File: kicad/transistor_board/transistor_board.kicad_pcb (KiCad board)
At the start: 2 copper layers, 25.4 x 38.1 mm, 17 parts, among them J1 Conn_01x10, J2 Conn_01x02, J3 Conn_01x02, Q1 MMBF170, Q2 MMBF170, Q3 MMBF170, Q4 MMBF170, U2 ESP32-cam, U3 LM7805_TO220

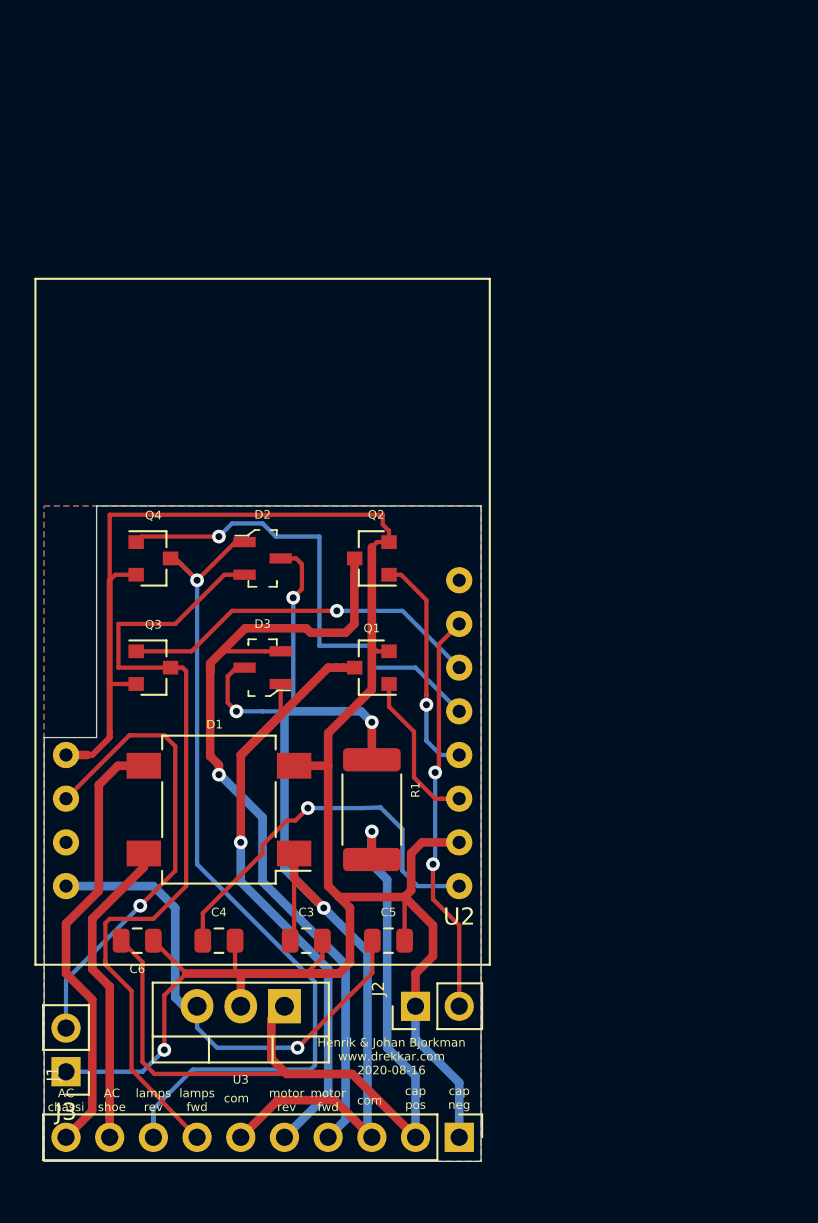
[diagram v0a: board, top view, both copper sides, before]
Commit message: Transistors failed, need to use bigger, such as D-Pak (TO252AA)
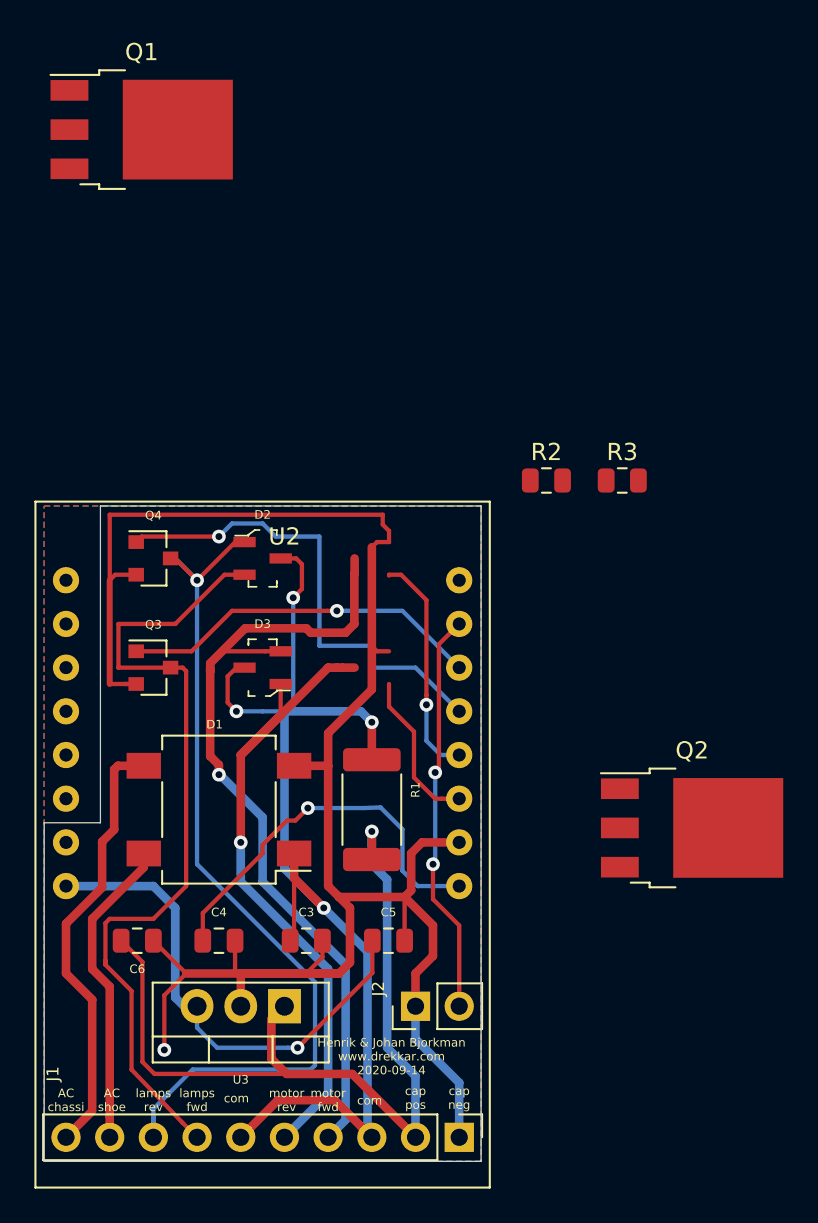
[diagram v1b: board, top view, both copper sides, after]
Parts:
- removed J3: Conn_01x02, Connector_PinHeader_2.54mm:PinHeader_1x02_P2.54mm_Vertical
- added R2: R, Resistor_SMD:R_0805_2012Metric, F.Cu at (142.2, 95.8)
- added R3: R, Resistor_SMD:R_0805_2012Metric, F.Cu at (146.6, 95.8)
- Q1, Q2: footprint Package_TO_SOT_SMD:SOT-23 -> Package_TO_SOT_SMD:TO-252-3_TabPin2
- U2: footprint eit_footprints:ESP32-CAM_12pin -> eit_footprints:ESP32-CAM
- moved Q1 34.0 mm to (118.7, 75.4), turned to 0 degrees
- moved Q2 24.3 mm to (150.7, 116.0), turned to 0 degrees
- moved U2 3.59 mm to (127.0, 109.2), turned to 0 degrees
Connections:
- U2 pad 13: GND -> Net-(U2-Pad13)
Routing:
- net Net-(U2-Pad14): track 27.2 -> 0.00 mm, vias 1 -> 0
- net Net-(U2-Pad12): track 0.00 -> 13.3 mm, vias 0 -> 1
- net Net-(Q2-Pad1): track 13.3 -> 0.00 mm, vias 1 -> 0
- net GND: track 140.3 -> 128.0 mm
- net Net-(U2-Pad11): track 0.00 -> 9.18 mm
- net Net-(Q1-Pad1): track 9.18 -> 0.00 mm
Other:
- outline, holes or cut-outs redrawn
- board text added: "Henrik & Johan Bjorkman www.drekkar.com 2020-09-14"
- board text removed: "Henrik & Johan Bjorkman www.drekkar.com 2020-08-16"

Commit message: Working on bigger transistors
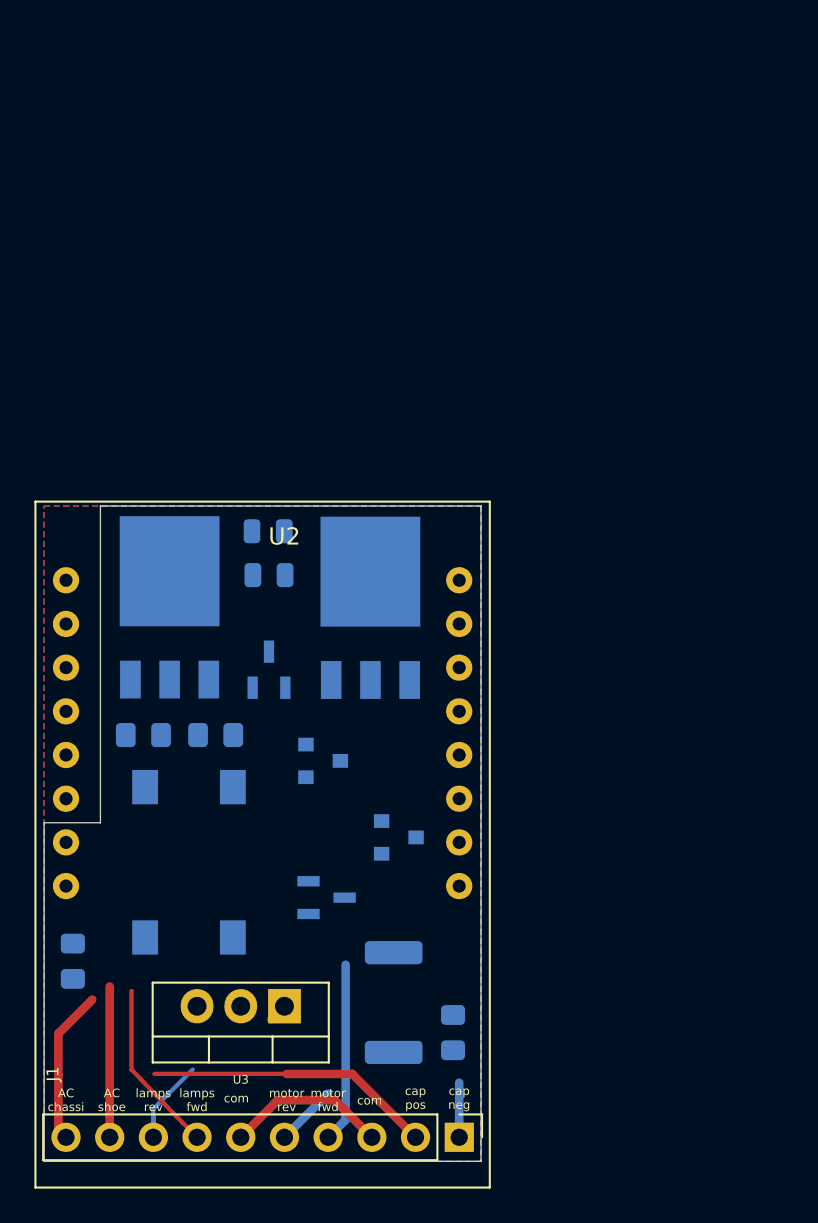
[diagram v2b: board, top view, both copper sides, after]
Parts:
- removed J2: Conn_01x02, Connector_PinHeader_2.54mm:PinHeader_1x02_P2.54mm_Vertical
- C3, C4, C5, C6: footprint Capacitor_SMD:C_0805_2012Metric -> Capacitor_SMD:C_0805_2012Metric_Pad1.15x1.40mm_HandSolder; moved to B.Cu
- D1, D2, D3, Q1, Q2, Q3, Q4, R1, R2, R3: moved to B.Cu
- moved Q2 33.0 mm to (120.3, 103.2), turned to 90 degrees
- moved Q1 30.8 mm to (132.0, 103.2), turned to 90 degrees
- moved R3 21.3 mm to (126.1, 101.3), turned to 180 degrees
- moved D2 20.1 mm to (129.4, 120.0)
- moved C6 19.1 mm to (136.8, 127.9), turned to 270 degrees
- moved C5 18.4 mm to (114.7, 123.8), turned to 270 degrees
- moved Q3 17.4 mm to (133.7, 116.5)
- moved R2 16.4 mm to (126.0, 98.8)
- moved Q4 15.4 mm to (129.2, 112.1)
- moved C3 13.1 mm to (123.0, 110.6)
- moved C4 12.7 mm to (118.8, 110.6)
- moved R1 11.3 mm to (133.3, 126.2), turned to 270 degrees
- moved D1 3.52 mm to (121.5, 118.0), turned to 270 degrees
- moved D3 0.39 mm to (126.1, 106.8), turned to 90 degrees
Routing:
- net GND: track 128.0 -> 3.18 mm, vias 1 -> 0
- net Net-(C3-Pad1): track 69.1 -> 9.77 mm, vias 4 -> 0
- net Net-(D2-Pad1): track 51.9 -> 6.09 mm, vias 1 -> 0
- net Net-(D2-Pad2): track 48.0 -> 10.1 mm
- net Net-(D3-Pad2): track 48.2 -> 10.5 mm, vias 1 -> 0
- net Net-(D3-Pad1): track 39.2 -> 3.59 mm, vias 1 -> 0
- net Net-(C6-Pad2): track 50.4 -> 17.5 mm, vias 1 -> 0
- net Net-(C5-Pad1): track 29.8 -> 0.76 mm, vias 1 -> 0
- net Net-(Q4-Pad1): track 28.3 -> 0.00 mm, vias 1 -> 0
- net Net-(J2-Pad2): track 23.5 -> 0.00 mm, vias 2 -> 0
- net Net-(C4-Pad1): track 22.6 -> 0.00 mm, vias 1 -> 0
- net Net-(Q3-Pad1): track 21.1 -> 0.00 mm, vias 1 -> 0
- net Net-(D1-Pad3): track 25.7 -> 9.01 mm
- net Net-(U2-Pad12): track 13.3 -> 0.00 mm, vias 1 -> 0
- net Net-(D1-Pad4): track 18.2 -> 8.76 mm
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
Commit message: Working on bigger transistors
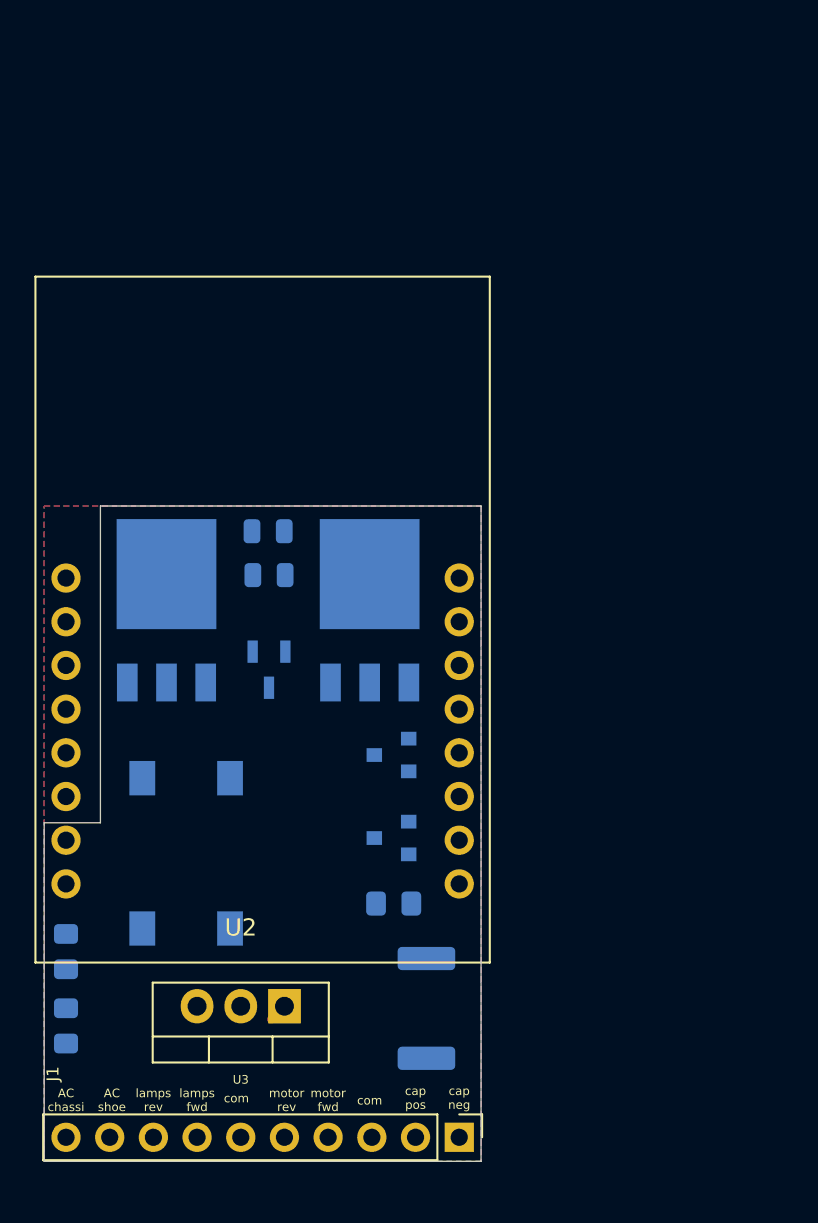
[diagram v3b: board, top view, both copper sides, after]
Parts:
- removed C4: C, Capacitor_SMD:C_0805_2012Metric_Pad1.15x1.40mm_HandSolder
- removed D2: D_x2_KCom_AAK, digikey-footprints:SOT-23-3
- moved C3 19.0 mm to (114.3, 127.5), turned to 90 degrees
- moved Q1 11.9 mm to (120.1, 103.3)
- moved Q2 11.6 mm to (132.0, 103.3)
- moved C6 8.26 mm to (133.3, 120.4), turned to 0 degrees
- moved Q4 3.99 mm to (133.2, 111.8), turned to 180 degrees
- moved U2 3.50 mm to (124.5, 111.6), turned to 180 degrees
- moved R1 1.94 mm to (135.3, 126.5), turned to 90 degrees
- moved C5 0.69 mm to (114.3, 123.2)
- moved D1 0.55 mm to (121.3, 117.5)
- moved Q3 0.43 mm to (133.2, 116.6), turned to 180 degrees
- turned D3 to 270 degrees
- turned R2 to 180 degrees
- turned R3 to 0 degrees
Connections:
- J1 pad 10: Net-(D1-Pad3) -> Net-(D1-Pad4)
- J1 pad 9: Net-(D1-Pad4) -> Net-(D1-Pad3)
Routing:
- net Net-(C6-Pad2): track 17.5 -> 1.08 mm
- net Net-(D3-Pad2): track 10.5 -> 0.00 mm
- net Net-(J1-Pad7): track 10.1 -> 0.00 mm
- net Net-(C3-Pad1): track 9.77 -> 0.00 mm
- net Net-(D1-Pad3): track 9.01 -> 0.00 mm
- net Net-(D1-Pad4): track 8.76 -> 0.64 mm
- net Net-(J1-Pad8): track 6.09 -> 0.00 mm
- net Net-(D3-Pad1): track 3.59 -> 0.00 mm
- net GND: track 3.18 -> 0.00 mm
- added copper zone on B.Cu, net GND
- added copper zone on F.Cu, net Net-(C3-Pad1)
- removed copper zone on F.Cu, net GND
- removed copper zone on B.Cu, net Net-(C3-Pad1)

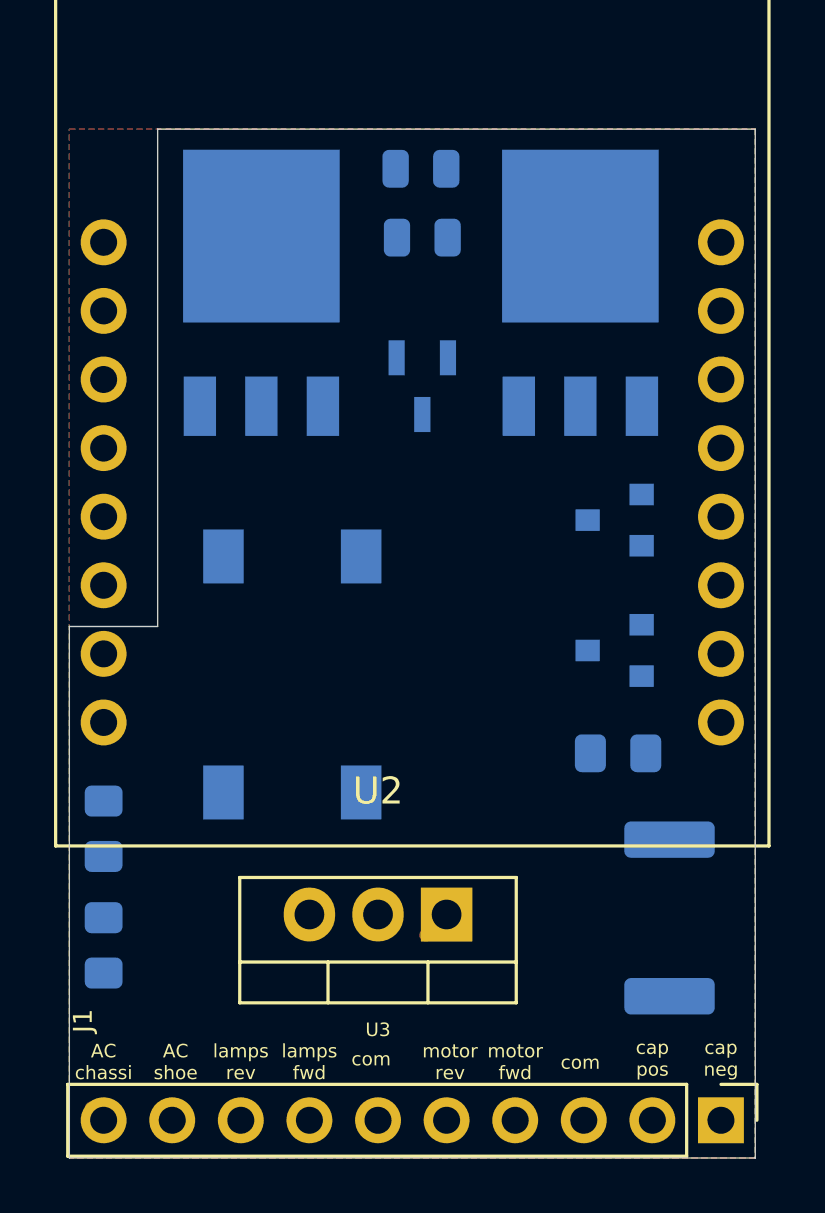
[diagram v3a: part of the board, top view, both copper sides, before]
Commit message: routing on transistor board
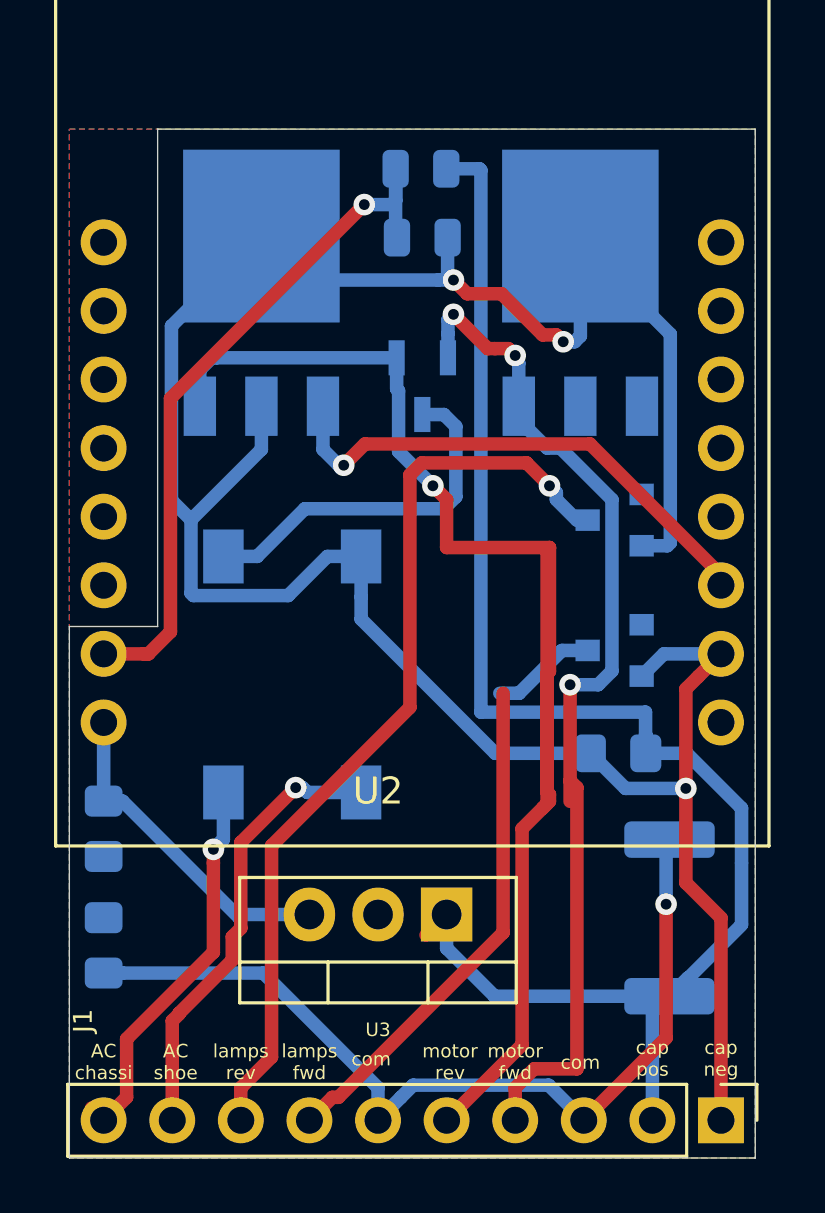
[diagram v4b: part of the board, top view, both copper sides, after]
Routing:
- net GND: track 0.00 -> 99.0 mm, vias 0 -> 3
- net Net-(D3-Pad1): track 0.00 -> 62.8 mm, vias 0 -> 1
- net Net-(C6-Pad2): track 1.08 -> 61.9 mm
- net Net-(C3-Pad1): track 0.00 -> 47.1 mm, vias 0 -> 1
- net Net-(D3-Pad2): track 0.00 -> 38.7 mm, vias 0 -> 3
- net Net-(J1-Pad8): track 0.00 -> 34.4 mm, vias 0 -> 1
- net Net-(R2-Pad2): track 0.00 -> 29.4 mm, vias 0 -> 1
- net Net-(J1-Pad7): track 0.00 -> 22.8 mm
- net Net-(Q1-Pad1): track 0.00 -> 19.3 mm, vias 0 -> 1
- net Net-(D1-Pad3): track 0.00 -> 16.8 mm, vias 0 -> 1
- net Net-(D1-Pad4): track 0.64 -> 14.6 mm, vias 0 -> 1
- net Net-(C5-Pad1): track 0.76 -> 13.1 mm
